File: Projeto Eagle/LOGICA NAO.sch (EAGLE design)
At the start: 5 parts, among them J1 CONECTOR_MACHO, J2 CONECTOR_FEMEA, U1 74HC132, U2 LM358D

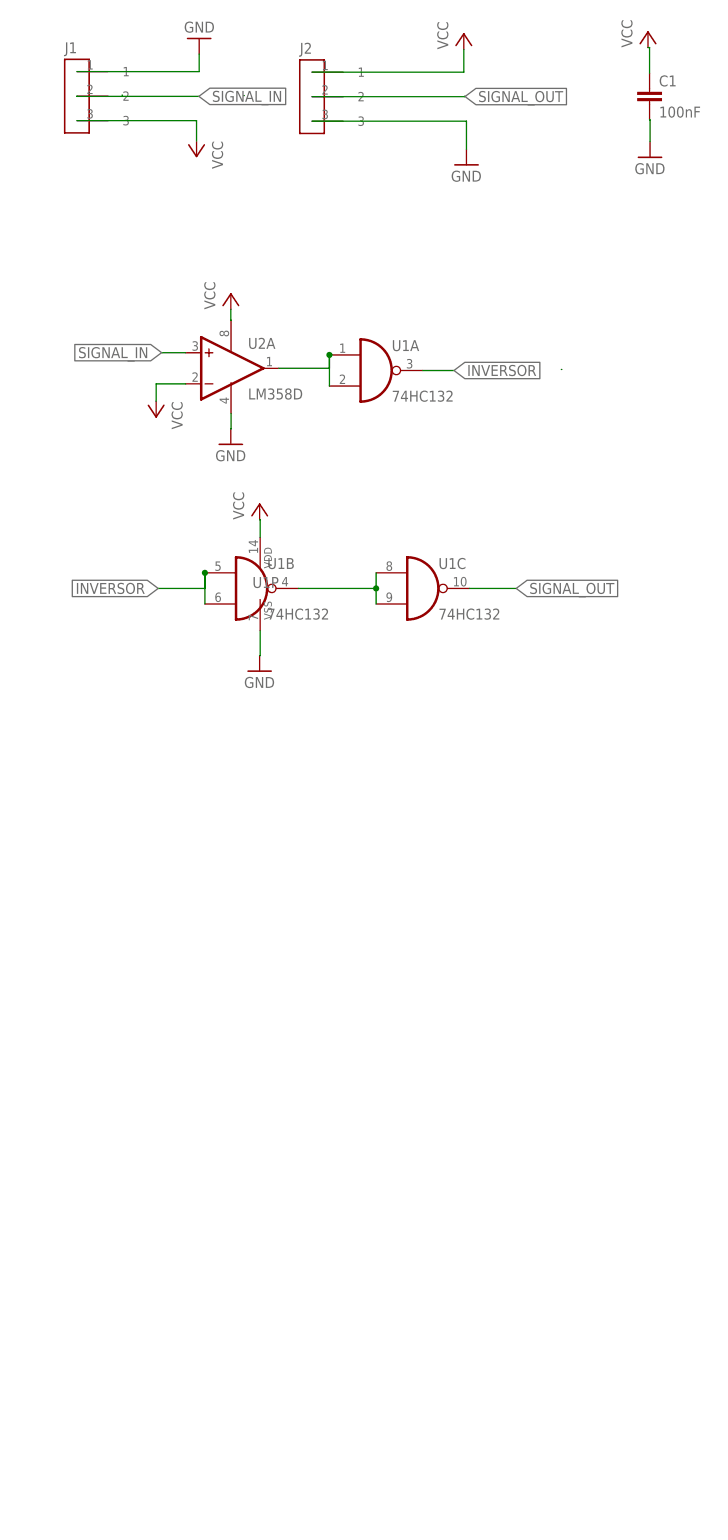
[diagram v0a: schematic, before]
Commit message: correção de pads e adição de label para versionamento
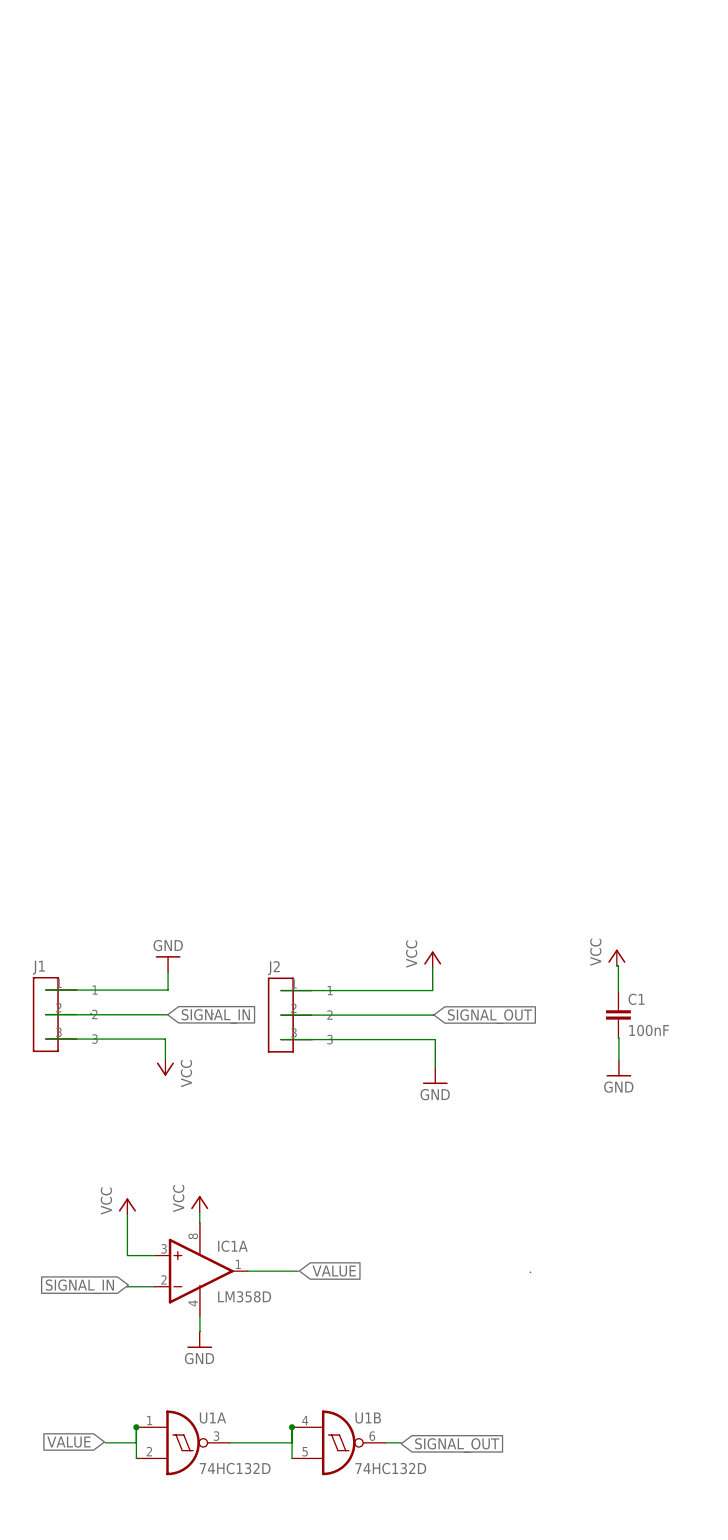
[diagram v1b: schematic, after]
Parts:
- removed U2: LM358D, linear:LM358D
- added IC1: LM358D, linear:LM358D
- U1: value 74HC132 -> 74HC132D; device 40xx:4011D -> 74xx-eu:74HC132D
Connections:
- net INVERSOR renamed N$4
- removed net N$3: U1A.I0, U1A.I1, U2A.OUT
- removed net N$4 (its old number): U1B.O, U1C.I0, U1C.I1
- new net VALUE: IC1A.OUT, U1A.I0, U1A.I1
- net GND: now also IC1P.V-; no longer U1P.VSS, U2P.V-
- net SIGNAL_IN: now also IC1A.-IN; no longer U2A.+IN
- net SIGNAL_OUT: now also U1B.O; no longer U1C.O
- net VCC: now also IC1A.+IN, IC1P.V+; no longer U1P.VDD, U2A.-IN, U2P.V+
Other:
- moved on the sheet: C1, J1, J2

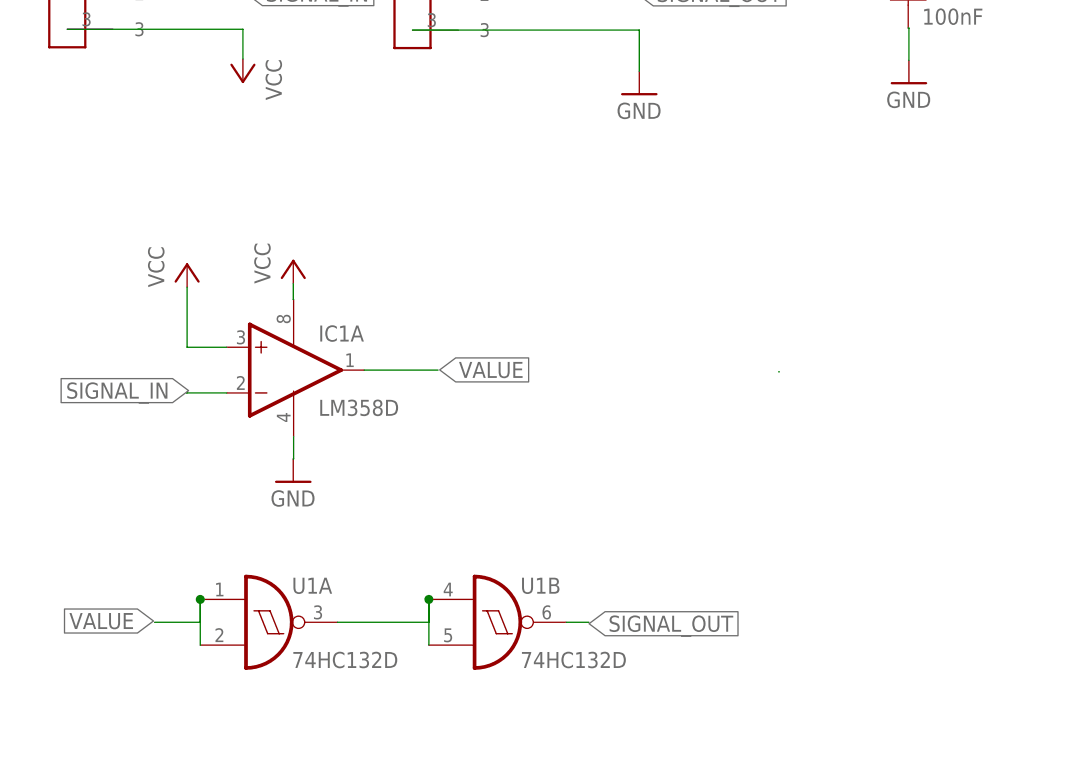
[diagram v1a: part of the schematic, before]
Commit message: correção de sensibilidade, reformulação de lógica, adição de plano VCC e atualização da BOM
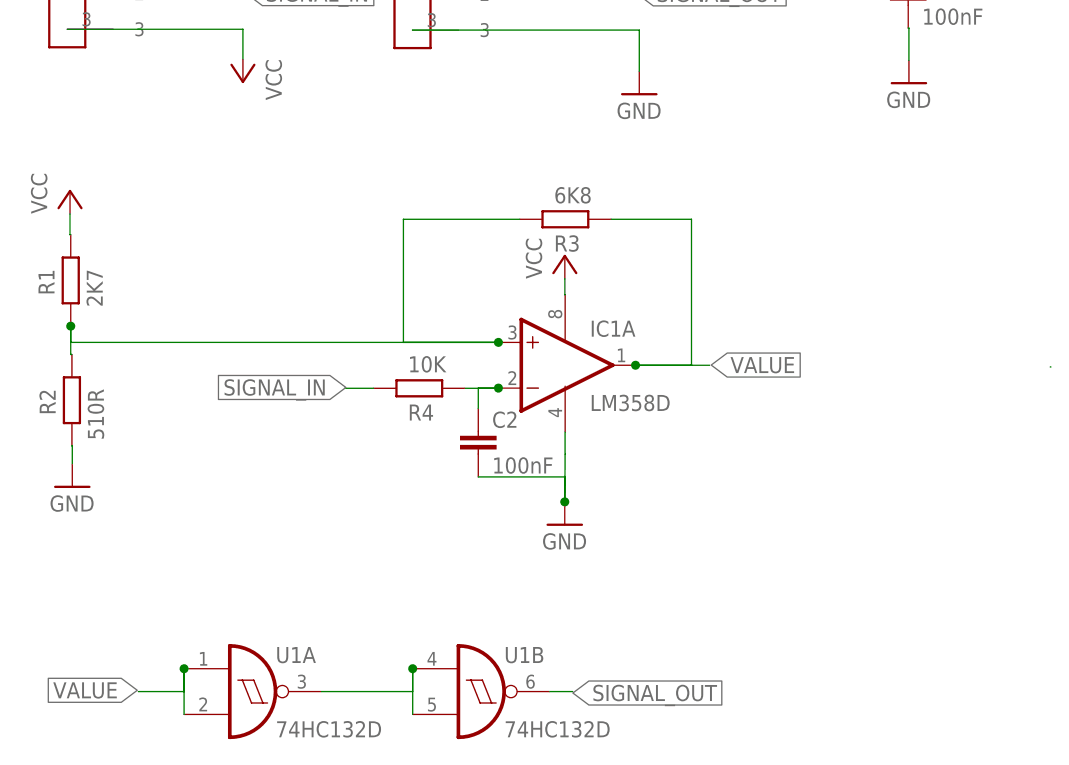
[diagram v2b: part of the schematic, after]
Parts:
- added C2: 100nF, rcl:C-EUC0805
- added R1: 2K7, rcl:R-EU_R0805W
- added R2: 510R, rcl:R-EU_R0805W
- added R3: 6K8, rcl:R-EU_R0805W
- added R4: 10K, rcl:R-EU_R0805W
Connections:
- new net N$3: C2.1, IC1A.-IN, R4.2
- new net N$5: IC1A.+IN, R1.2, R2.1, R3.1
- net GND: now also C2.2, R2.2
- net SIGNAL_IN: now also R4.1; no longer IC1A.-IN
- net VALUE: now also R3.2
- net VCC: now also R1.1; no longer IC1A.+IN
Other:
- moved on the sheet: IC1A, U1A, U1B
